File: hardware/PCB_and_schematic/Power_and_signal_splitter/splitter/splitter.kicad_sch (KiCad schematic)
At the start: 0 parts

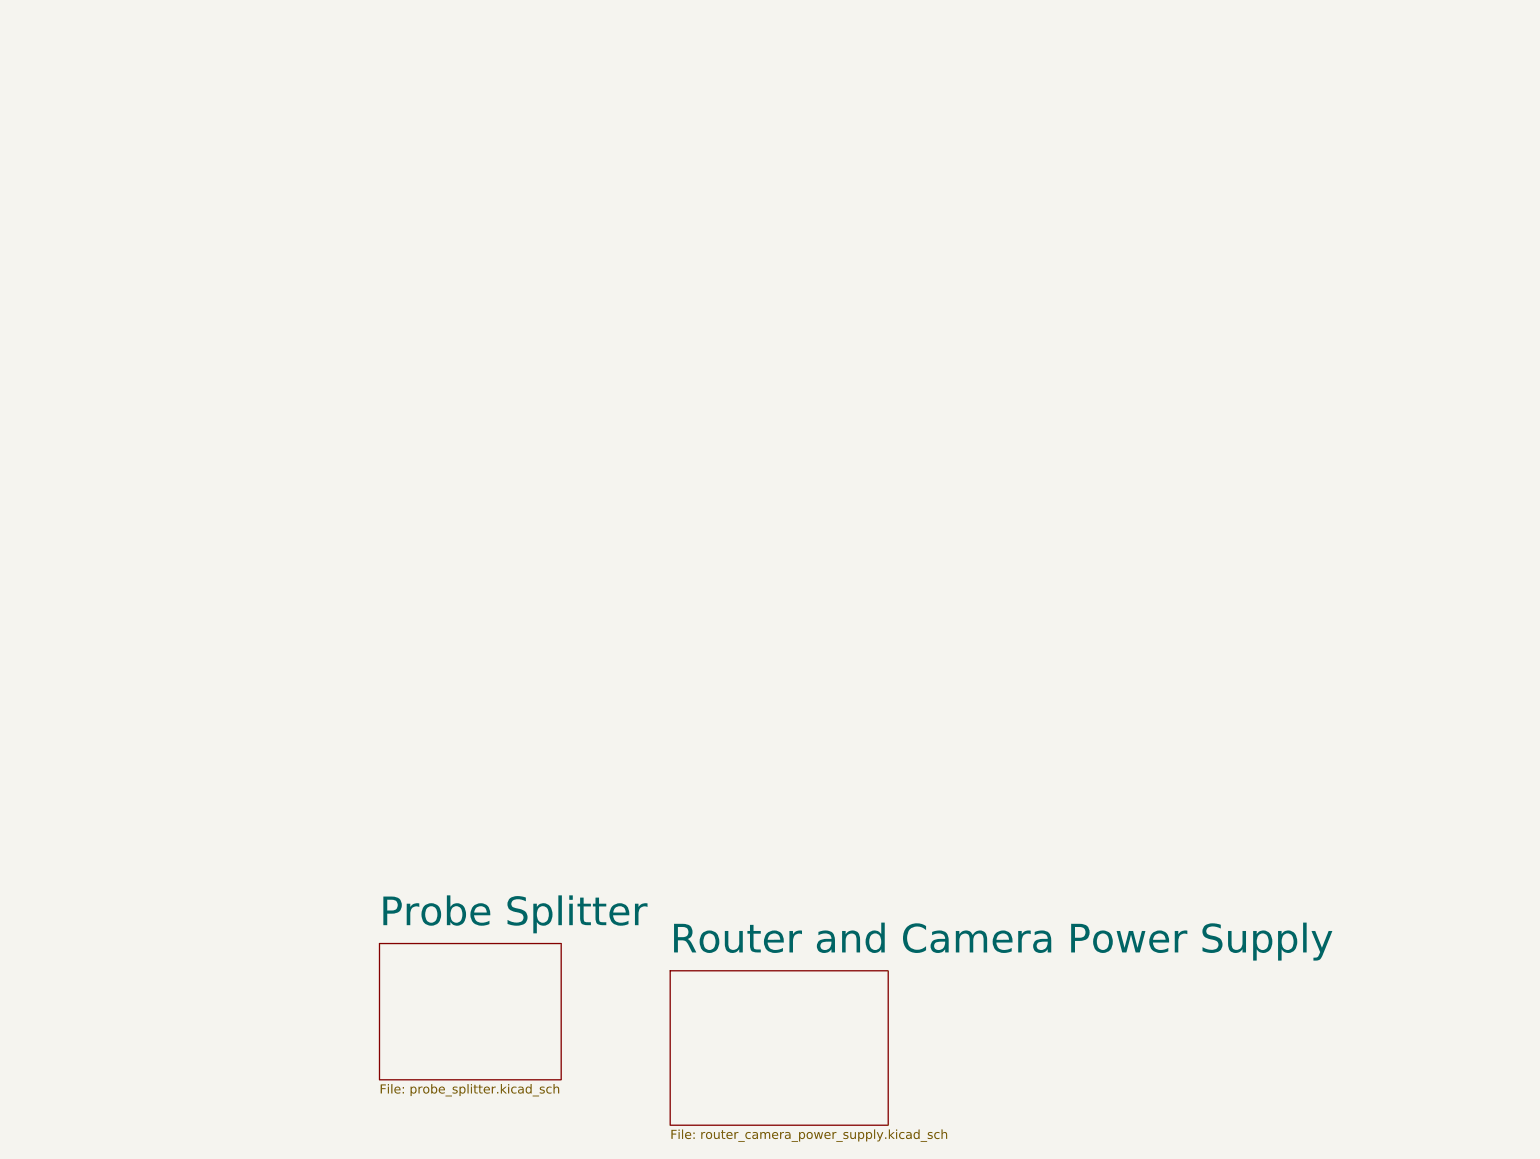
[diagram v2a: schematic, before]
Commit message: Splitter and connector footprints, progress with balancer pcb routing
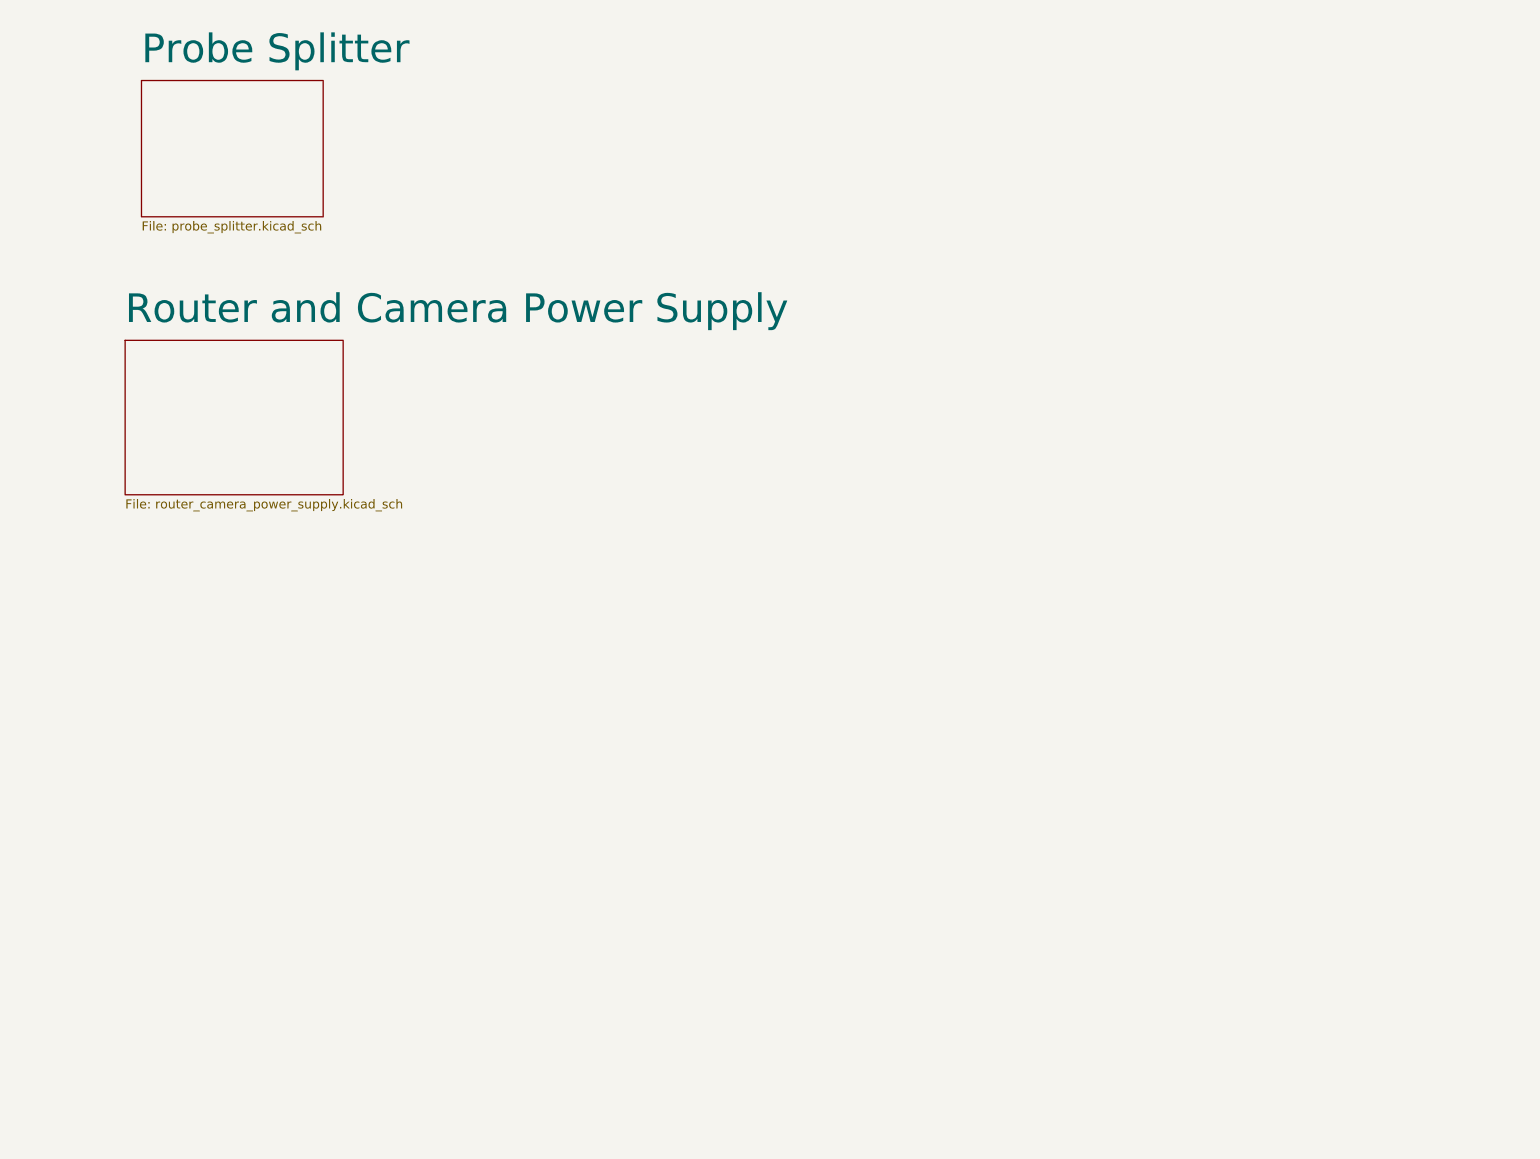
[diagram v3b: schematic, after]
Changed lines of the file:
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@@
 	(paper "A4")
 	(sheet
-		(at 106.68 152.4)
+		(at 30.48 64.262)
 		(size 30.48 21.59)
 		(fields_autoplaced yes)
@@
 		)
 		(property "Sheetname" "Router and Camera Power Supply"
-			(at 106.68 150.3234 0)
+			(at 30.48 62.1854 0)
 			(effects
 				(font
@@
 		)
 		(property "Sheetfile" "router_camera_power_supply.kicad_sch"
-			(at 106.68 174.5746 0)
+			(at 30.48 86.4366 0)
 			(effects
 				(font
@@
 	)
 	(sheet
-		(at 66.04 148.59)
+		(at 32.766 27.94)
 		(size 25.4 19.05)
 		(fields_autoplaced yes)
@@
 		)
 		(property "Sheetname" "Probe Splitter"
-			(at 66.04 146.5134 0)
+			(at 32.766 25.8634 0)
 			(effects
 				(font
@@
 		)
 		(property "Sheetfile" "probe_splitter.kicad_sch"
-			(at 66.04 168.2246 0)
+			(at 32.766 47.5746 0)
 			(effects
 				(font

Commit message: done LT3652
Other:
- removed sheet Router and Camera Power Supply
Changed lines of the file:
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@@
 	(paper "A4")
-	(sheet
-		(at 30.48 64.262)
-		(size 30.48 21.59)
-		(fields_autoplaced yes)
-		(stroke
-			(width 0.1524)
-			(type solid)
-		)
-		(fill
-			(color 0 0 0 0.0000)
-		)
-		(property "Sheetname" "Router and Camera Power Supply"
-			(at 30.48 62.1854 0)
-			(effects
-				(font
-					(size 4 4)
-				)
-				(justify left bottom)
-			)
-		)
-		(property "Sheetfile" "router_camera_power_supply.kicad_sch"
-			(at 30.48 86.4366 0)
-			(effects
-				(font
-					(size 1.27 1.27)
-				)
-				(justify left top)
-			)
-		)
-		(instances
-			(project "splitter"
-				(path "/0286cab7-ab30-426b-8345-1f03e11d2c7c"
-					(page "3")
-				)
-			)
-		)
-	)
 	(sheet
 		(at 32.766 27.94)
